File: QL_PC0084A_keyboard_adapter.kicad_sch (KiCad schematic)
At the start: 29 parts, among them J1 Turned Pins 1x20, J2 Turned Pins 1x20, J3 Male Horz. 6pin, J4 Fem. 6P, J5 DIN-5 Female, J6 DIN-6, Q1 NPN, Q2 NPN, U1 SOCKET 40 PIN, U2 D8749HC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

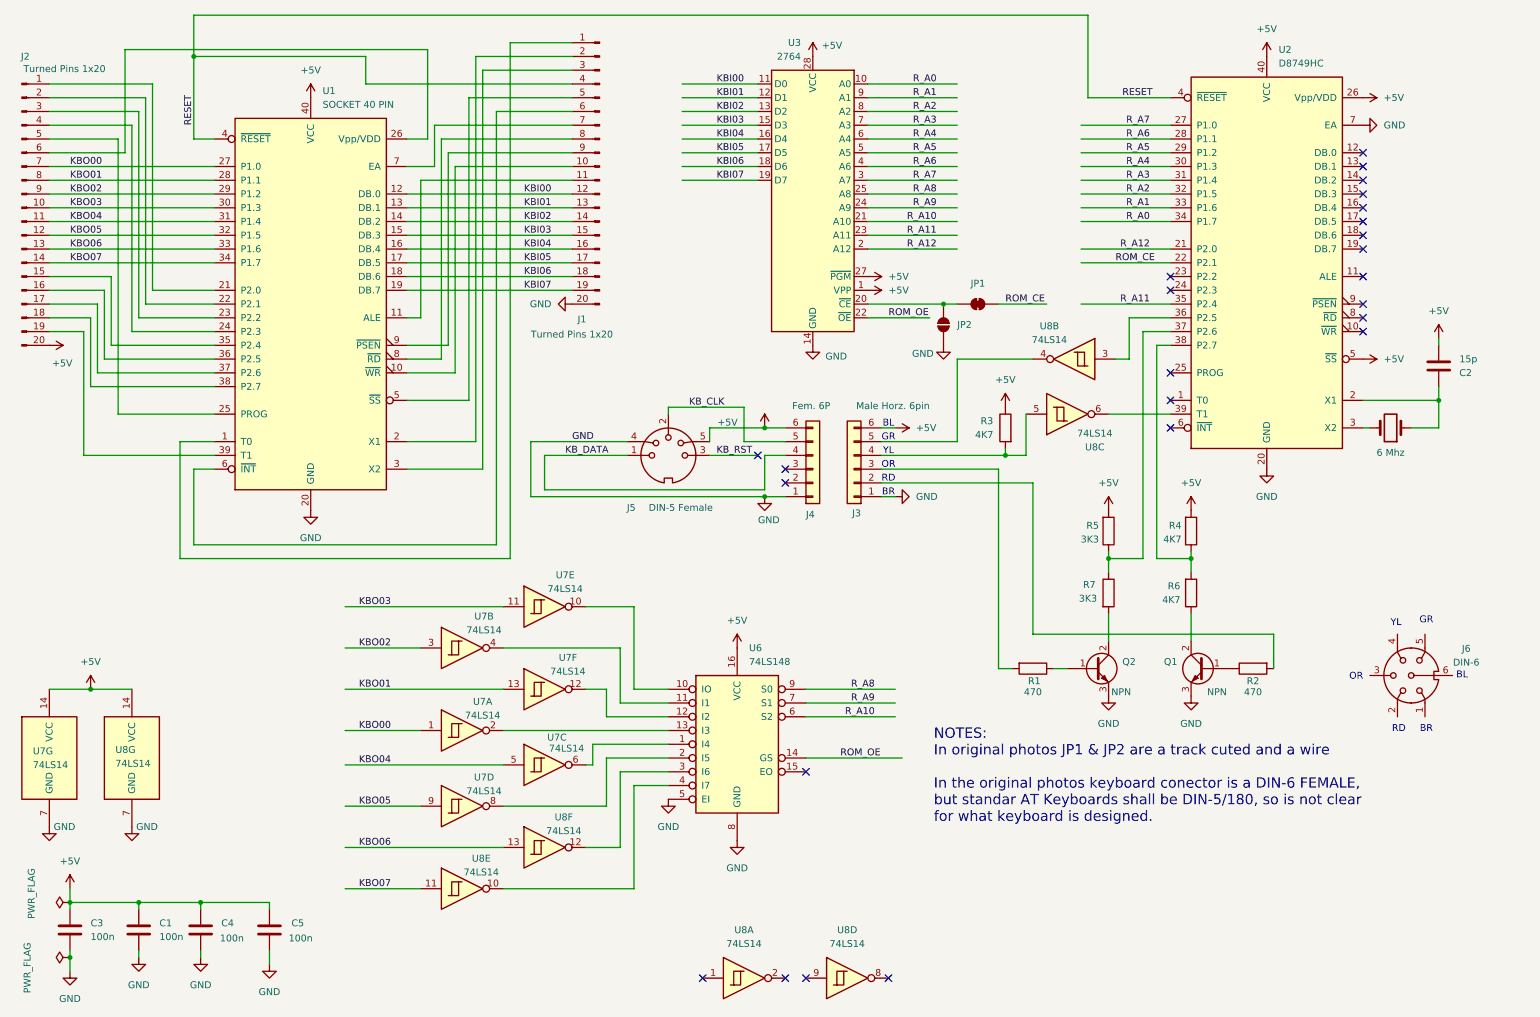
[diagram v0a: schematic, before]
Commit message: update information about transistors
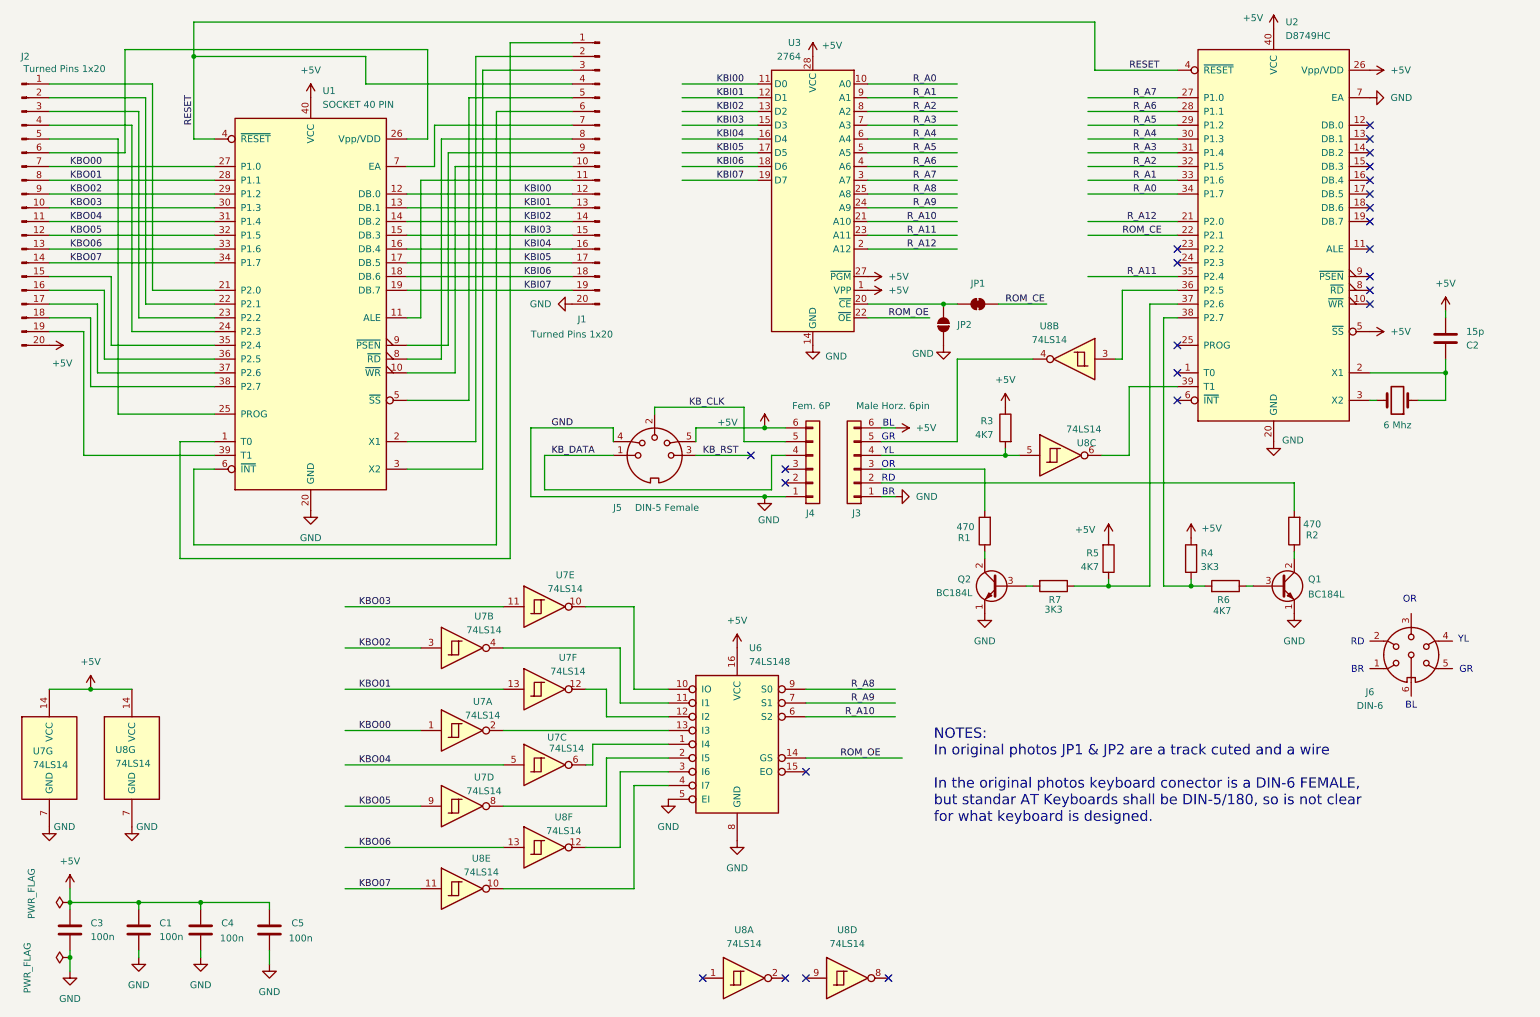
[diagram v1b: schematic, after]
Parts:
- Q1, Q2: value NPN -> BC184L; symbol Device:Q_NPN_BCE -> Device:Q_NPN_ECB
- R4: value 4K7 -> 3K3
- R5: value 3K3 -> 4K7
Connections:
- net GND: now also Q1.1 (E), Q2.1 (E); no longer Q1.3 (E), Q2.3 (E)
- net at R1.1: now also Q2.2 (C); no longer Q2.1 (B)
- net at R7.2: now also Q2.3 (B); no longer Q2.2 (C)
- net at R2.1: now also Q1.2 (C); no longer Q1.1 (B)
- net at R6.1: now also Q1.3 (B); no longer Q1.2 (C)
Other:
- moved on the sheet: C2, J5, J6, Q1, Q2, R1, R2, R4, R5, R6, R7, U2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
